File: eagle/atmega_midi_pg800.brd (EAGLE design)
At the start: 101.9 x 80.8 mm, 44 parts, among them IC2 4067N, IC3 4067N, IC4 4067N, IC5 7805TV, Q1 16.000Mhz, U1 6N138, U2 ATMEGA328P_PDIP

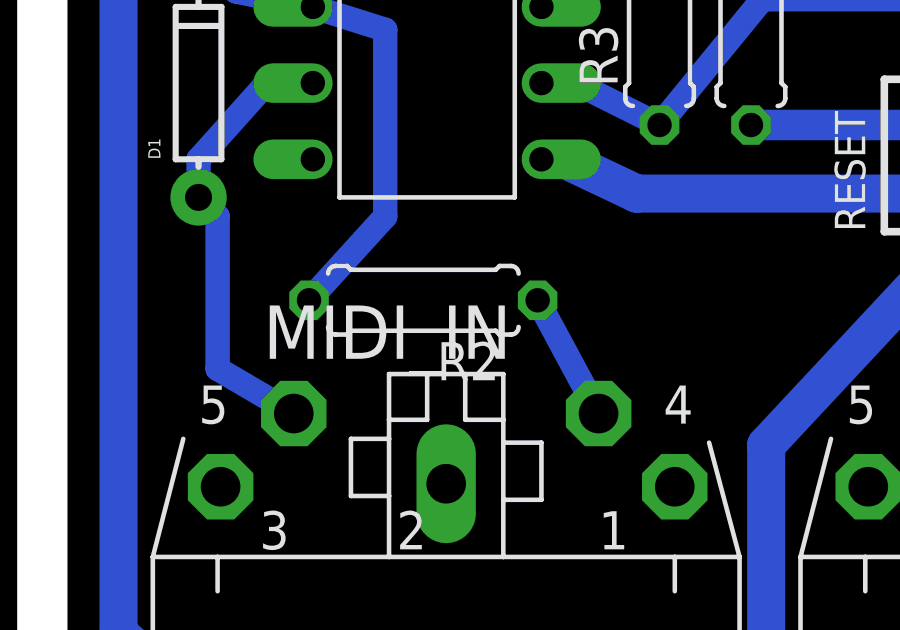
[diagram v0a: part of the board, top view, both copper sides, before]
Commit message: moved a resistor away from midi in jack
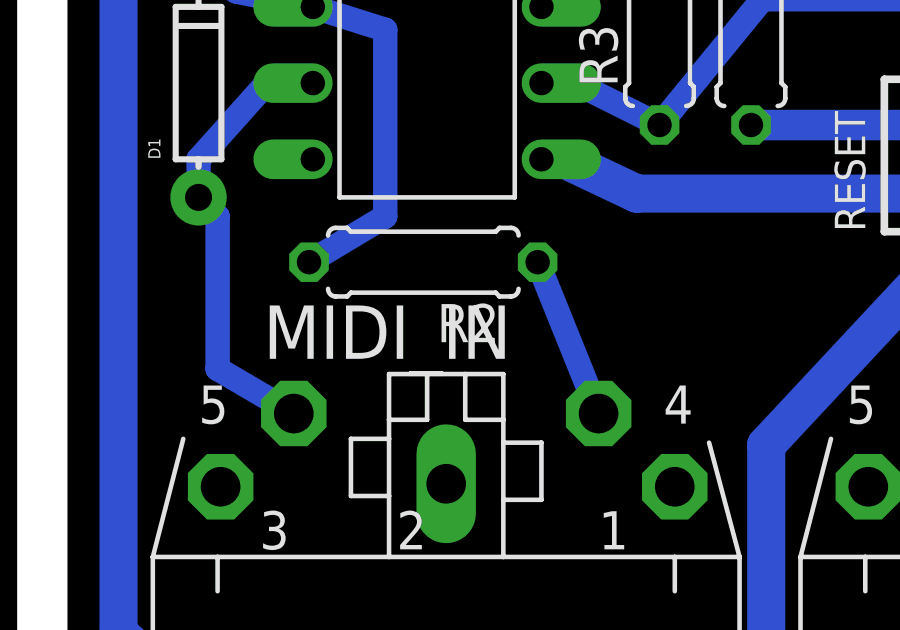
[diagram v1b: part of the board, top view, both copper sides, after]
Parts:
- moved R2 1.27 mm to (11.9, 20.1)
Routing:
- net N$8: track 4.29 -> 5.44 mm
- net N$7: track 16.6 -> 15.8 mm
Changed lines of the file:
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@@
 </element>
 <element name="R1" library="rcl" package="0207/7" value="10k" x="22.86" y="28.448" rot="R270"/>
-<element name="R2" library="rcl" package="0207/7" value="220" x="11.938" y="18.796" rot="R180"/>
+<element name="R2" library="rcl" package="0207/7" value="220" x="11.938" y="20.066" rot="R180"/>
 <element name="R24" library="rcl" package="0207/7" value="1M" x="64.77" y="17.78" rot="R270"/>
 <element name="R3" library="rcl" package="0207/7" value="270" x="19.812" y="28.448" rot="R90"/>
@@
 <contactref element="R2" pad="2"/>
 <wire x1="10.668" y1="27.813" x2="10.668" y2="21.59" width="0.8128" layer="16"/>
-<wire x1="10.668" y1="21.59" x2="8.128" y2="18.796" width="0.8128" layer="16"/>
+<wire x1="10.668" y1="21.59" x2="8.128" y2="20.066" width="0.8128" layer="16"/>
 <wire x1="8.255" y1="28.575" x2="10.668" y2="27.813" width="0.8128" layer="16"/>
 <wire x1="5.715" y1="29.083" x2="4.445" y2="29.845" width="0.8128" layer="16"/>
@@
 <contactref element="R2" pad="1"/>
 <contactref element="MIDI_IN" pad="4"/>
-<wire x1="17.78" y1="15.02" x2="15.748" y2="18.796" width="0.8128" layer="16"/>
+<wire x1="17.78" y1="15.02" x2="15.748" y2="20.066" width="0.8128" layer="16"/>
 </signal>
 <signal name="+5V">
